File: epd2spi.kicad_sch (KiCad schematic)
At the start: 22 parts, among them J1 EPD_FPC, J2 Conn_01x08, Q1 SI1308EDL

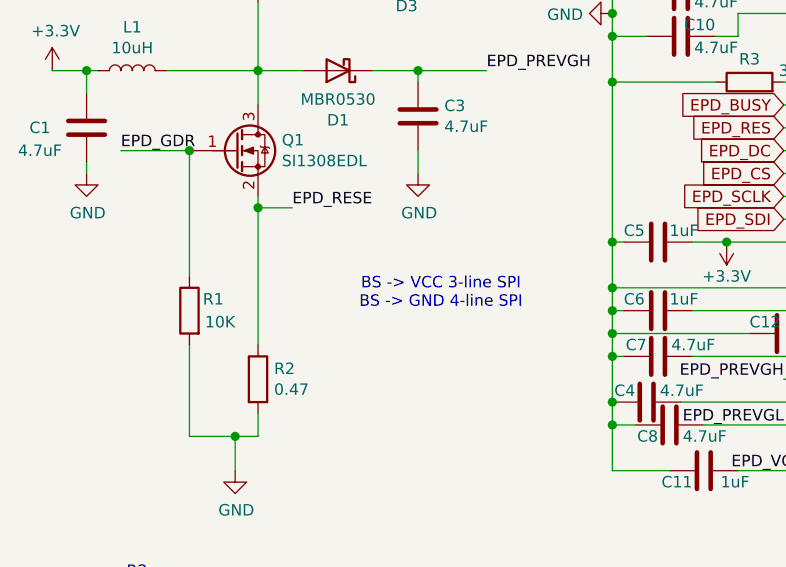
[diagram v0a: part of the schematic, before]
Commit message: Change the size and re-route
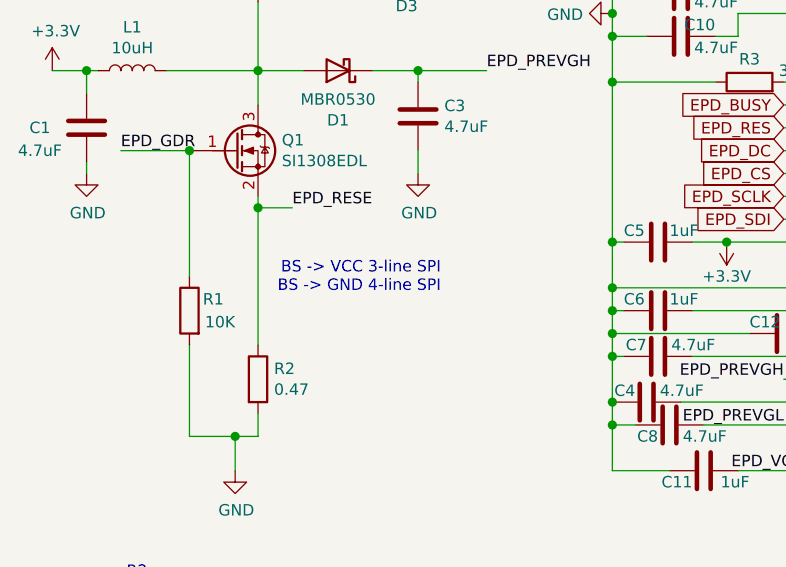
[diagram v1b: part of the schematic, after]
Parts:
- R2, R3: footprint Resistor_SMD:R_0603_1608Metric -> Resistor_SMD:R_0805_2012Metric
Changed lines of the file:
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@@
   )
   (text "BS -> VCC 3-line SPI\nBS -> GND 4-line SPI" (at 129.54 116.205 180)
-    (effects (font (size 1.27 1.27)))
+    (effects (font (size 1.27 1.27)) (justify right bottom))
   )
   (label "EPD_GDR" (at 93.98 100.33 0)
@@
       (effects (font (size 1.27 1.27)) (justify left))
     )
-    (property "Footprint" "Resistor_SMD:R_0603_1608Metric" (id 2) (at 107.442 125.73 90)
+    (property "Footprint" "Resistor_SMD:R_0805_2012Metric" (id 2) (at 107.442 125.73 90)
       (effects (font (size 1.27 1.27)) hide)
     )
@@
     (property "Reference" "R3" (id 0) (at 163.83 90.17 90))
     (property "Value" "3" (id 1) (at 167.64 91.44 90))
-    (property "Footprint" "Resistor_SMD:R_0603_1608Metric" (id 2) (at 163.83 94.488 90)
+    (property "Footprint" "Resistor_SMD:R_0805_2012Metric" (id 2) (at 163.83 94.488 90)
       (effects (font (size 1.27 1.27)) hide)
     )
@@
     )
     (path "/147167a8-31b7-4f3a-b554-4c6af56ee35f"
-      (reference "R2") (unit 1) (value "0.47") (footprint "Resistor_SMD:R_0603_1608Metric")
+      (reference "R2") (unit 1) (value "0.47") (footprint "Resistor_SMD:R_0805_2012Metric")
     )
     (path "/48c791a2-c19d-4e77-a261-0aa6db18b9a1"
-      (reference "R3") (unit 1) (value "3") (footprint "Resistor_SMD:R_0603_1608Metric")
-    )
-  )
+      (reference "R3") (unit 1) (value "3") (footprint "Resistor_SMD:R_0805_2012Metric")
+    )
+  )
